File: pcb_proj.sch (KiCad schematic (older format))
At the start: 2 parts, among them J1 Conn_02x32_Top_Bottom, J2 Conn_02x10_Top_Bottom

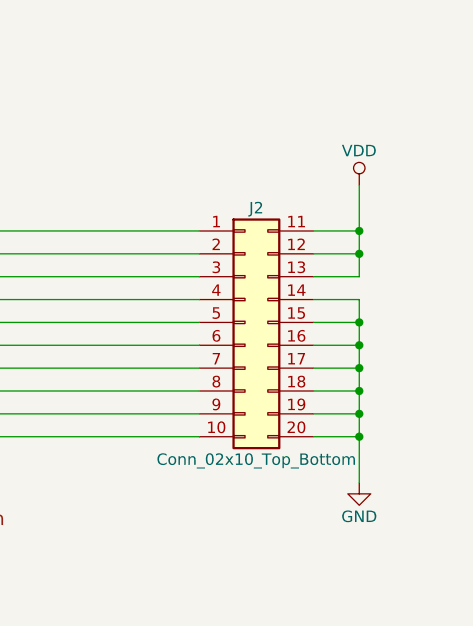
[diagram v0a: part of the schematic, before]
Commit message: fixed all ERC errors
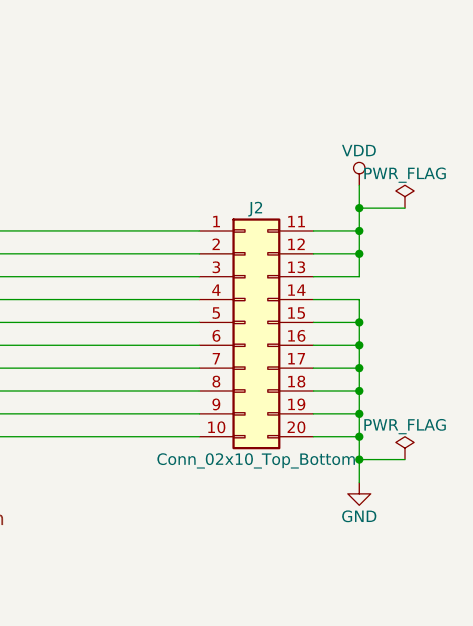
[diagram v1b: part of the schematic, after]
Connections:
- wire segments 160 -> 162
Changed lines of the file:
@@
 Text Label 1700 5200 0    60   ~ 0
 C31
+$Comp
+L PWR_FLAG #FLG03
+U 1 1 5CA0FB8A
+P 10000 3350
+F 0 "#FLG03" H 10000 3425 50  0001 C CNN
+F 1 "PWR_FLAG" H 10000 3500 50  0000 C CNN
+F 2 "" H 10000 3350 50  0001 C CNN
+F 3 "" H 10000 3350 50  0001 C CNN
+	1    10000 3350
+	1    0    0    -1
+$EndComp
+$Comp
+L PWR_FLAG #FLG04
+U 1 1 5CA1000E
+P 10000 4450
+F 0 "#FLG04" H 10000 4525 50  0001 C CNN
+F 1 "PWR_FLAG" H 10000 4600 50  0000 C CNN
+F 2 "" H 10000 4450 50  0001 C CNN
+F 3 "" H 10000 4450 50  0001 C CNN
+	1    10000 4450
+	1    0    0    -1
+$EndComp
+Wire Wire Line
+	10000 3350 9800 3350
+Connection ~ 9800 3350
+Wire Wire Line
+	10000 4450 9800 4450
+Connection ~ 9800 4450
 $EndSCHEMATC
